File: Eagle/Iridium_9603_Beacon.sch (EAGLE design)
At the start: 64 parts, among them J1 SS4-10-3.50-X-D, Q1 DMG3415U-7, U1 MCP111T-195I/TT, U2 SPX3819-3.3, U3 LTC3225EDDB#TRMPBF, U4 MPL3115A2LGA8, U5 ATSAMD21G18_QFN, U6 SAM-M8Q, X1 32.768

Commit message: Initial update for V4 - still work in progress
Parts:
- removed GND.: (no value), adafruit:PINHD-1X1
- added C18: 10nF, microbuilder:CAP_CERAMIC0805-NOOUTLINE
- added C19: 10uF, microbuilder:CAP_CERAMIC0805-NOOUTLINE
- added CON4: uFL, microbuilder:ANTENNA_U.FL
- added D4: MBR120, microbuilder:DIODE-SCHOTTKYSOD-123
- added GND2, GND3, VBUS: (no value), adafruit:PINHD-1X1
- added GNSS, IRIDIUM: SMA-142-0711-821/826, con-coax:SMA-142-0711-821/826
- added JP2: JUMPER-PAD-3-2OF3_NC_BY_TRACE_LARGE, SparkFun-Passives:JUMPER-PAD-3-2OF3_NC_BY_TRACE_LARGE
- added L1: 33nH, microbuilder:FERRITE-0805NO
- added LED2: RED, microbuilder:LED0805_NOOUTLINE
- added R10: 2.2K, microbuilder:RESISTOR_0603_NOOUT
- added R11: 30K, microbuilder:RESISTOR0805_NOOUTLINE
- added R9: 10 ohm, microbuilder:RESISTOR0805_NOOUTLINE
- added U7: LT1634-1,25BMCMS8, linear-technology:LT1634-1,25BMCMS8
- BAT1, BAT2, BAT3: device SparkFun-Electromechanical:BATTERYKEYSTONE82 -> SparkFun-Electromechanical:BATTERYKEYSTONE92
- LED1: value RED -> (none); device microbuilder:LED0805_NOOUTLINE -> SparkFun-LED:WS2812B
- R2: value 30K -> 12K
- R7: value 2.2K -> 47k
- U1: value MCP111T-195I/TT -> MCP111T-240E/TT; MPN (none) -> MCP111T-240E/TT
- U6: value SAM-M8Q -> MAX-M8; device ubloxLib:SAM-M8Q -> ubloxLib:MAX-M8
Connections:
- new net GPS_ANT: GNSS.1, L1.P$2, U6.11_RF_IN
- new net N$1: C18.1, L1.P$1, R9.1
- new net N$16: CON1.VBUS, D4.A
- new net N$17: JP2.3, R2.2
- new net N$18: JP2.1, R11.2
- new net N$3: LED2.A, R10.2
- new net VCC_RF: R9.2, U6.14_VCC_RF
- net +3V3: now also C19.1, LED1.VDD, U6.6_V_BCKP; no longer U6.V_BCKP
- net 3V3SW: now also U6.7_VCC_IO, U6.8_VCC; no longer U6.VCC, U6.VCC_IO
- net A0: now also R7.2, U7.VOUT
- net D0: now also U6.2_TXD; no longer U6.TXD
- net D1: now also U6.3_RXD; no longer U6.RXD
- net D13: now also LED1.DIN, R10.1; no longer R7.1
- net GND: now also C18.2, C19.2, CON4.GND@0, CON4.GND@1, GND2.1, GND3.1, GNSS.2, IRIDIUM.2, LED1.VSS, LED2.C, R11.1, U6.10_GND, U6.12_GND, U6.1_GND, U7.GND; no longer GND..1, LED1.C, U6.GND
- net N$11: now also JP2.2; no longer R2.2
- net N$2: now also CON4.SIGNAL, IRIDIUM.1; no longer LED1.A, R7.2
- net VBUS: now also D4.C, R7.1, VBUS.1; no longer CON1.VBUS
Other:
- note added: "150mA"
- note added: "3 x AA Energiser Ultimate Lithium in Keystone Electronics 92 clips"
- note added: "60mA"
- note added: "Iridium 9603 Beacon Notes"
- note added: "LEDs"
- note added: "Notes on power voltages: MBR120 diode has a forward voltage drop of approx.: 0.26V at 170mA 0.19V at 12mA MBR120 diode plus SPX3819-3.3 regulator have a combined voltage drop of approx.: 0.22V at 12mA; 0.36V at 170mA. Output starts to collapse when 'solar' voltage drops below approx.: 3.65V at 12mA; 3.80V at 170mA. Reported voltage on A7 will bottom out at 3.38V / 3.43V even though the actual vol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"
- note added: "V4: Power: 3 x AA batteries in Keystone 92 clips GNSS: u-blox MAX-M8Q with SMA antenna SMA antenna for 9603N Added WS2812B LED Added LT1634-1,25BMCMS8 voltage reference to allow low battery voltages to be measured Added protection diode for USB power Added split pad to select supercapacitor charge current"
- note added: "WS2812B"
- note added: "u-blox MAX-M8Q"
- note removed: "3 x AAA Energiser Ultimate Lithium in Keystone Electronics 82 clips"
- note removed: "LED"
- note removed: "u-blox SAM-M8Q"

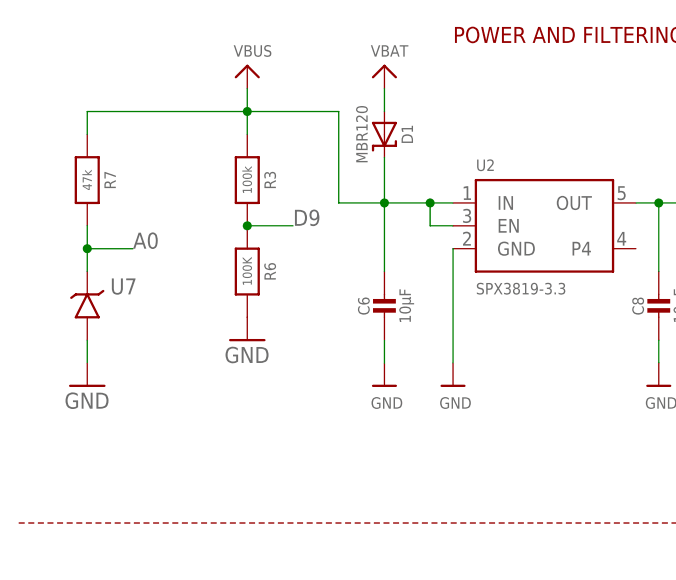
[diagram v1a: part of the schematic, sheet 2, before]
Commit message: Included full details of RockBLOCK gateway messaging
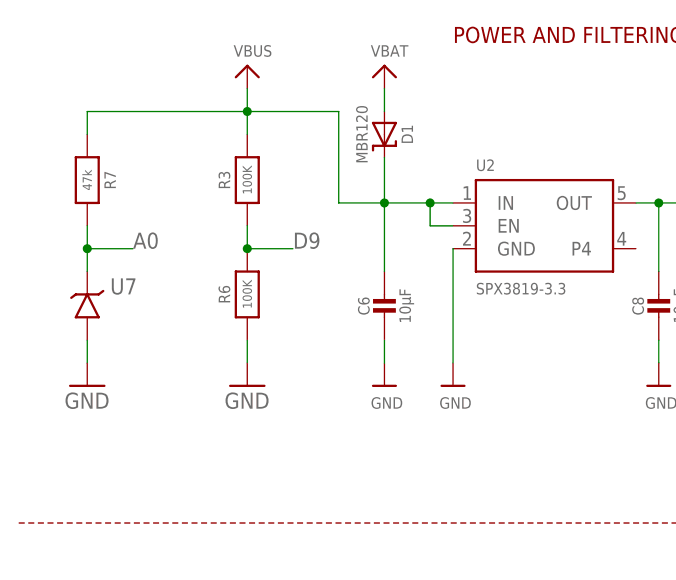
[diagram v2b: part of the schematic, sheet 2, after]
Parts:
- C13: device microbuilder:CAP_CERAMIC0603_NO -> microbuilder:CAP_CERAMIC0805-NOOUTLINE
- R3: value 100k -> 100K; device microbuilder:RESISTOR_0603_NOOUT -> microbuilder:RESISTOR0805_NOOUTLINE
- R6: device microbuilder:RESISTOR_0603_NOOUT -> microbuilder:RESISTOR0805_NOOUTLINE
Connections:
- net D9: now also R3.1, R6.2; no longer R3.2, R6.1
- net GND: now also R6.1; no longer R6.2
- net VBUS: now also R3.2; no longer R3.1
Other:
- moved on the sheet: R3, R6
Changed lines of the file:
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@@
 <part name="U2" library="microbuilder" deviceset="VREG_SOT23-5" device="" value="SPX3819-3.3"/>
 <part name="D1" library="microbuilder" deviceset="DIODE-SCHOTTKY" device="SOD-123" value="MBR120"/>
-<part name="R3" library="microbuilder" deviceset="RESISTOR" device="_0603_NOOUT" value="100k"/>
-<part name="R6" library="microbuilder" deviceset="RESISTOR" device="_0603_NOOUT" value="100K"/>
 <part name="GND13" library="supply1" library_urn="urn:adsk.eagle:library:371" deviceset="GND" device=""/>
 <part name="U5" library="microbuilder" deviceset="ATSAMD21J" device="_QFN" value="ATSAMD21G18_QFN"/>
@@
 <part name="+3V9" library="supply1" library_urn="urn:adsk.eagle:library:371" deviceset="+3V3" device=""/>
 <part name="+3V10" library="supply1" library_urn="urn:adsk.eagle:library:371" deviceset="+3V3" device=""/>
-<part name="C13" library="microbuilder" deviceset="CAP_CERAMIC" device="0603_NO" value="0.1uF"/>
 <part name="JP1" library="SparkFun-Passives" deviceset="JUMPER-PAD-3-2OF3_NC_BY_TRACE" device="_LARGE" value=""/>
 <part name="U$4" library="microbuilder" deviceset="VBUS" device=""/>
@@
 <part name="R11" library="microbuilder" deviceset="RESISTOR" device="0805_NOOUTLINE" value="30K"/>
 <part name="U$1" library="microbuilder" deviceset="GND" device=""/>
+<part name="C13" library="microbuilder" deviceset="CAP_CERAMIC" device="0805-NOOUTLINE" value="0.1uF"/>
+<part name="R3" library="microbuilder" deviceset="RESISTOR" device="0805_NOOUTLINE" value="100K"/>
+<part name="R6" library="microbuilder" deviceset="RESISTOR" device="0805_NOOUTLINE" value="100K"/>
 </parts>
 <sheets>
@@
 <instance part="D1" gate="G$1" x="45.72" y="160.02" rot="R270"/>
 <instance part="FRAME1" gate="G$1" x="0" y="0"/>
-<instance part="R3" gate="G$1" x="30.48" y="154.94" rot="R270"/>
-<instance part="R6" gate="G$1" x="30.48" y="144.78" rot="R270"/>
-<instance part="GND13" gate="1" x="30.48" y="137.16"/>
+<instance part="GND13" gate="1" x="30.48" y="132.08"/>
 <instance part="U5" gate="G$1" x="50.8" y="58.42"/>
 <instance part="U$5" gate="G$1" x="25.4" y="15.24"/>
@@
 <instance part="U$45" gate="G$1" x="243.84" y="160.02"/>
 <instance part="D4" gate="G$1" x="243.84" y="149.86" rot="R90"/>
+<instance part="R3" gate="G$1" x="30.48" y="154.94" rot="R90"/>
+<instance part="R6" gate="G$1" x="30.48" y="142.24" rot="R90"/>
 </instances>
 <busses>
@@
 </segment>
 <segment>
-<pinref part="R6" gate="G$1" pin="2"/>
 <pinref part="GND13" gate="1" pin="GND"/>
+<wire x1="30.48" y1="134.62" x2="30.48" y2="137.16" width="0.1524" layer="91"/>
+<pinref part="R6" gate="G$1" pin="1"/>
 </segment>
 <segment>
@@
 <wire x1="40.64" y1="162.56" x2="40.64" y2="152.4" width="0.1524" layer="91"/>
 <wire x1="40.64" y1="152.4" x2="45.72" y2="152.4" width="0.1524" layer="91"/>
-<pinref part="R3" gate="G$1" pin="1"/>
 <wire x1="30.48" y1="160.02" x2="30.48" y2="162.56" width="0.1524" layer="91"/>
 <junction x="30.48" y="162.56"/>
@@
 <wire x1="30.48" y1="162.56" x2="12.7" y2="162.56" width="0.1524" layer="91"/>
 <wire x1="12.7" y1="162.56" x2="12.7" y2="160.02" width="0.1524" layer="91"/>
+<pinref part="R3" gate="G$1" pin="2"/>
 </segment>
 <segment>
@@
 </segment>
 <segment>
-<pinref part="R3" gate="G$1" pin="2"/>
-<pinref part="R6" gate="G$1" pin="1"/>
-<wire x1="30.48" y1="149.86" x2="35.56" y2="149.86" width="0.1524" layer="91"/>
-<junction x="30.48" y="149.86"/>
-<label x="35.56" y="149.86" size="1.778" layer="95"/>
+<wire x1="30.48" y1="147.32" x2="35.56" y2="147.32" width="0.1524" layer="91"/>
+<junction x="30.48" y="147.32"/>
+<label x="35.56" y="147.32" size="1.778" layer="95"/>
+<wire x1="30.48" y1="147.32" x2="30.48" y2="149.86" width="0.1524" layer="91"/>
+<pinref part="R6" gate="G$1" pin="2"/>
+<pinref part="R3" gate="G$1" pin="1"/>
 </segment>
 </net>
@@
 <instance part="+3V9" gate="G$1" x="152.4" y="152.4" rot="MR0"/>
 <instance part="+3V10" gate="G$1" x="160.02" y="127" rot="MR0"/>
-<instance part="C13" gate="G$1" x="104.14" y="101.6"/>
 <instance part="U$41" gate="G$1" x="91.44" y="106.68"/>
 <instance part="U$18" gate="G$1" x="104.14" y="93.98"/>
 <instance part="U$42" gate="G$1" x="111.76" y="93.98"/>
+<instance part="C13" gate="G$1" x="104.14" y="101.6"/>
 </instances>
 <busses>
@@
 </segment>
 <segment>
+<pinref part="U$18" gate="G$1" pin="GND"/>
 <pinref part="C13" gate="G$1" pin="2"/>
-<pinref part="U$18" gate="G$1" pin="GND"/>
-<wire x1="104.14" y1="99.06" x2="104.14" y2="96.52" width="0.1524" layer="91"/>
+<wire x1="104.14" y1="96.52" x2="104.14" y2="99.06" width="0.1524" layer="91"/>
 </segment>
 <segment>
@@
 <segment>
 <pinref part="U4" gate="G$1" pin="CAP"/>
+<wire x1="121.92" y1="109.22" x2="104.14" y2="109.22" width="0.1524" layer="91"/>
 <pinref part="C13" gate="G$1" pin="1"/>
-<wire x1="121.92" y1="109.22" x2="104.14" y2="109.22" width="0.1524" layer="91"/>
 <wire x1="104.14" y1="109.22" x2="104.14" y2="106.68" width="0.1524" layer="91"/>
 </segment>
